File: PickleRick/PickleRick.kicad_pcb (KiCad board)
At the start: 4 copper layers, 100 x 37 mm, 176 parts, among them J1 Conn_01x06_Male, J10 Conn_01x03_Male, J11 Conn_01x02_Male, J12 Conn_01x05_Male, J14 DeployLipo, J15 UCLipo, J16 Conn_Coaxial, J17 USB_C_Receptacle_USB2.0, J18 Conn_Coaxial, J2 Conn_01x02_Male, J3 Conn_01x02_Male, J4 Micro_SD_Card_Det, J5 CON7_1X7_DRH_HPI125_TYC, J6 Screw_Terminal_01x08, Q1 MMDT2222A, Q10 AO3401A, Q2 PMV20ENR, Q3 NCV8415STT1G, Q4 NCV8415STT1G, Q5 NCV8415STT1G, Q6 NCV8415STT1G, Q7 SI4143DY-T1-GE3, Q8 SI4143DY-T1-GE3, Q9 AO3401A, U1 SN65HVD230, U10 LTC4411ES5TRMPBF, U11 LTC4411ES5TRMPBF, U12 LT1963AxST-3.3, U13 LTC4412xS6, U14 LTC4412xS6, U15 LTC4412xS6, U16 LTC4412xS6, U17 MAX-M8Q, U18 CP2102-GMR-QFN28, U19 RFM95W-868S2, U2 ESP32-WROOM-32D, U3 MS5607-02BA, U4 LTV-247, U5 PCA9534RGVR, U6 PCA9685BS, U7 H3LIS100DLTR, U8 ICM-20608-G, U9 MMC5983MA

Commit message: removed some vias to conform to jlcpcb 100k holes per sqm
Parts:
- moved REF** 43.6 mm to (147.9, 79.0), turned to 180 degrees
- moved G*** 1.93 mm to (167.2, 79.7), turned to -90 degrees
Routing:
- net GND: track 162.7 -> 158.1 mm, vias 264 -> 189
- net /LORA_INT: track 120.4 -> 119.3 mm
- net /nukes/Nuke2: track 30.6 -> 29.8 mm
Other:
- board text added: "NUKES"
- board text removed: "PYROS"

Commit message: pcikle
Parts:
- moved J10 0.25 mm to (109.1, 62.1)

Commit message: final changes to pick rick
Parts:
- C1: value 1nF -> 0.1uF
- J5: value CON7_1X7_DRH_HPI125_TYC -> 292227-7
- moved TP30 1.42 mm to (164.9, 89.0)
- moved D20 1.30 mm to (163.9, 86.7)
- moved TP31 1.18 mm to (162.7, 89.0)
- moved TP1 0.55 mm to (171.0, 86.7)
- moved U18 0.45 mm to (173.8, 93.0)
- moved R1 0.36 mm to (172.8, 86.8)
- moved R2 0.24 mm to (177.3, 87.1)
- moved R5 0.12 mm to (179.1, 87.1)
- turned C30 to 90 degrees
- turned C32 to -90 degrees
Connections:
- C30 pad 1: GND -> +3V3
- C30 pad 2: +3V3 -> GND
- D20 pad 3: /usb_uart/Data- -> /usb_uart/Data+
- D20 pad 4: /usb_uart/Data+ -> /usb_uart/Data-
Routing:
- net /CAN_LOW: track 14.2 -> 21.1 mm
- net /usb_uart/Data-: track 20.0 -> 25.1 mm, vias 0 -> 1
- net /CAN_HIGH: track 19.0 -> 21.1 mm
- net +3V3: track 100.3 -> 98.8 mm
- net GND: track 158.4 -> 157.0 mm, vias 189 -> 188
- net /power/RBUS_3.3_IN: track 29.2 -> 28.1 mm
- net /RXD: track 30.6 -> 31.4 mm
- net /RTS: track 14.8 -> 15.5 mm
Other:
- board text added: "+-"
- board text added: "-+"
- board text added: "0"
- board text added: "1"
- board text added: "2"
- board text added: "3"
- board text added: "GND"
- board text added: "GPS"
- board text added: "LORA"
- board text added: "SCL"
- board text added: "SDA"

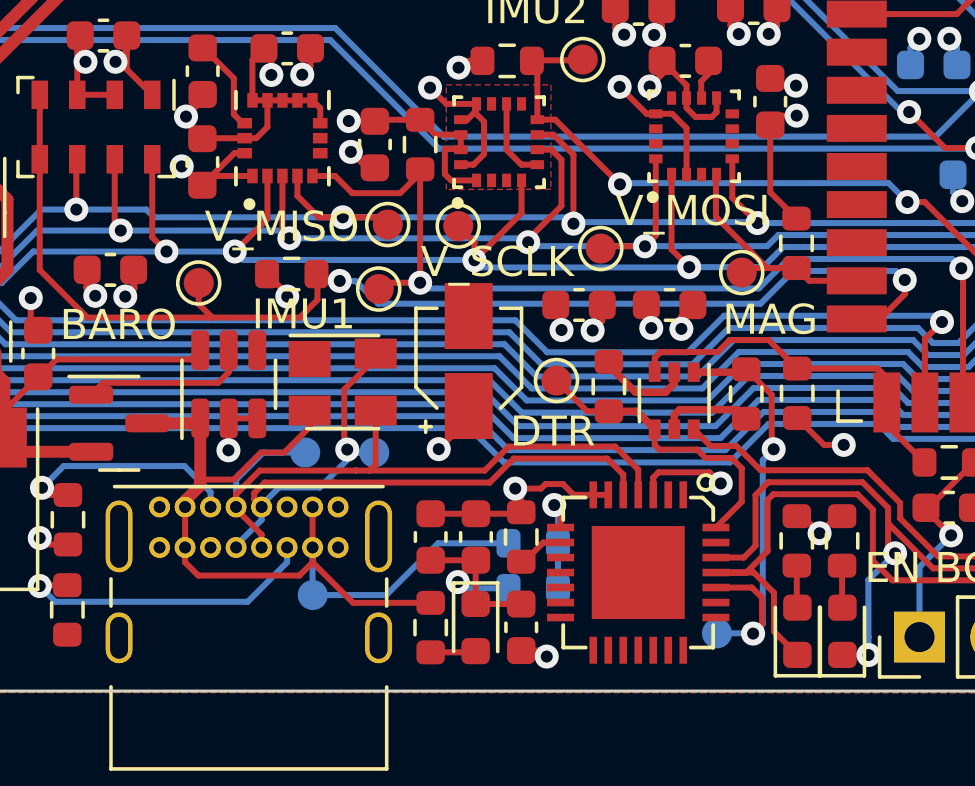
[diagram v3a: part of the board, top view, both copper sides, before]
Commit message: switched vspi and hspi labels so they are consistent with documentation
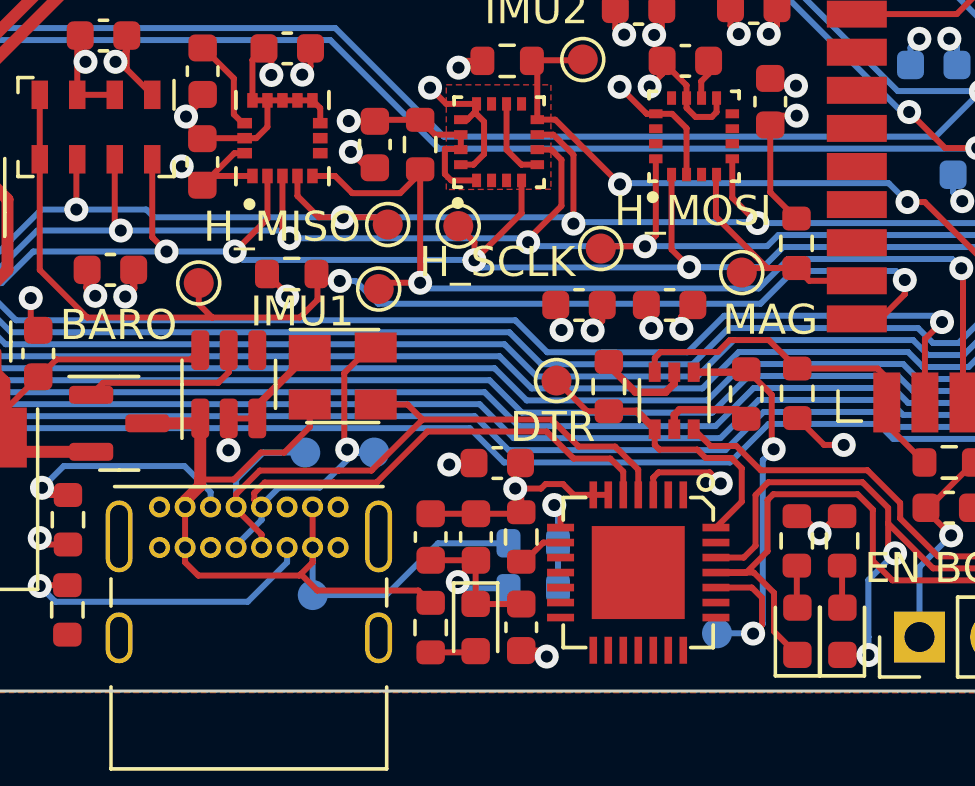
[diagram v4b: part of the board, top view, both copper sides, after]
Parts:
- C30: footprint Capacitor_SMD:CP_Elec_3x5.3 -> Capacitor_SMD:C_0603_1608Metric
- U7: value H3LIS100DLTR -> H3LIS331DLTR
- moved C30 3.53 mm to (169.1, 89.4), turned to 180 degrees
- moved D20 0.20 mm to (163.9, 86.5)
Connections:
- J4 pad 3: /HSPI_MOSI -> /VSPI_MOSI
- J4 pad 5: /HSPI_SCLK -> /VSPI_SCLK
- J4 pad 7: /HSPI_MISO -> /VSPI_MISO
- J5 pad 3: /HSPI_MOSI -> /VSPI_MOSI
- J5 pad 5: /HSPI_SCLK -> /VSPI_SCLK
- J5 pad 6: /HSPI_MISO -> /VSPI_MISO
- TP11 pad 1: /VSPI_MISO -> /HSPI_MISO
- TP12 pad 1: /VSPI_MOSI -> /HSPI_MOSI
- TP13 pad 1: /VSPI_SCLK -> /HSPI_SCLK
- TP17 pad 1: /HSPI_SCLK -> /VSPI_SCLK
- TP18 pad 1: /HSPI_MISO -> /VSPI_MISO
- TP19 pad 1: /HSPI_MOSI -> /VSPI_MOSI
- U19 pad 2: /VSPI_MISO -> /HSPI_MISO
- U19 pad 3: /VSPI_MOSI -> /HSPI_MOSI
- U19 pad 4: /VSPI_SCLK -> /HSPI_SCLK
- U2 pad 13: /VSPI_SCLK -> /HSPI_SCLK
- U2 pad 14: /VSPI_MISO -> /HSPI_MISO
- U2 pad 16: /VSPI_MOSI -> /HSPI_MOSI
- U2 pad 30: /HSPI_SCLK -> /VSPI_SCLK
- U2 pad 31: /HSPI_MISO -> /VSPI_MISO
- U2 pad 37: /HSPI_MOSI -> /VSPI_MOSI
- U3 pad 6: /VSPI_MISO -> /HSPI_MISO
- U3 pad 7: /VSPI_MOSI -> /HSPI_MOSI
- U3 pad 8: /VSPI_SCLK -> /HSPI_SCLK
- U7 pad 4: /VSPI_SCLK -> /HSPI_SCLK
- U7 pad 6: /VSPI_MOSI -> /HSPI_MOSI
- U7 pad 7: /VSPI_MISO -> /HSPI_MISO
- U8 pad 2: /VSPI_SCLK -> /HSPI_SCLK
- U8 pad 3: /VSPI_MOSI -> /HSPI_MOSI
- U8 pad 4: /VSPI_MISO -> /HSPI_MISO
- U9 pad 1: /VSPI_SCLK -> /HSPI_SCLK
- U9 pad 16: /VSPI_MOSI -> /HSPI_MOSI
- U9 pad 5: /VSPI_MISO -> /HSPI_MISO
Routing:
- net /VSPI_MISO: track 105.4 -> 74.7 mm, vias 6 -> 2
- net /HSPI_MISO: track 74.7 -> 105.4 mm, vias 2 -> 6
- net /VSPI_SCLK: track 100.2 -> 70.5 mm, vias 6 -> 2
- net /HSPI_SCLK: track 70.5 -> 100.2 mm, vias 2 -> 6
- net /VSPI_MOSI: track 99.6 -> 88.4 mm, vias 6 -> 2
- net /HSPI_MOSI: track 88.4 -> 99.6 mm, vias 2 -> 6
- net GND: track 157.0 -> 160.8 mm, vias 188 -> 189
- net /usb_uart/Data-: track 25.1 -> 26.2 mm
- net +3V3: track 98.8 -> 97.9 mm, vias 44 -> 43
